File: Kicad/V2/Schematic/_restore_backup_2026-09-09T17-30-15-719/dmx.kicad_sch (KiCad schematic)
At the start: 12 parts, among them J6 XLR5_Ground, U6 B0505S-1W1, U7 6N137, U8 MAX485E

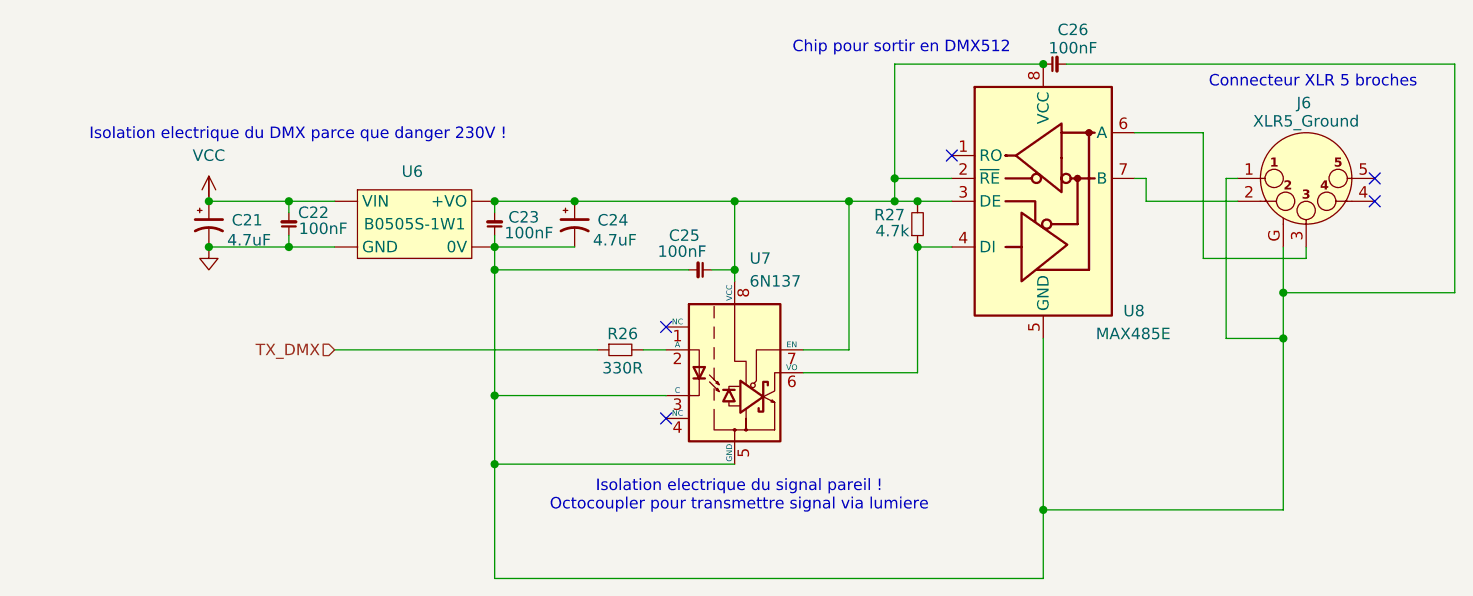
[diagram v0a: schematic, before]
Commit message: finition schematic de reference
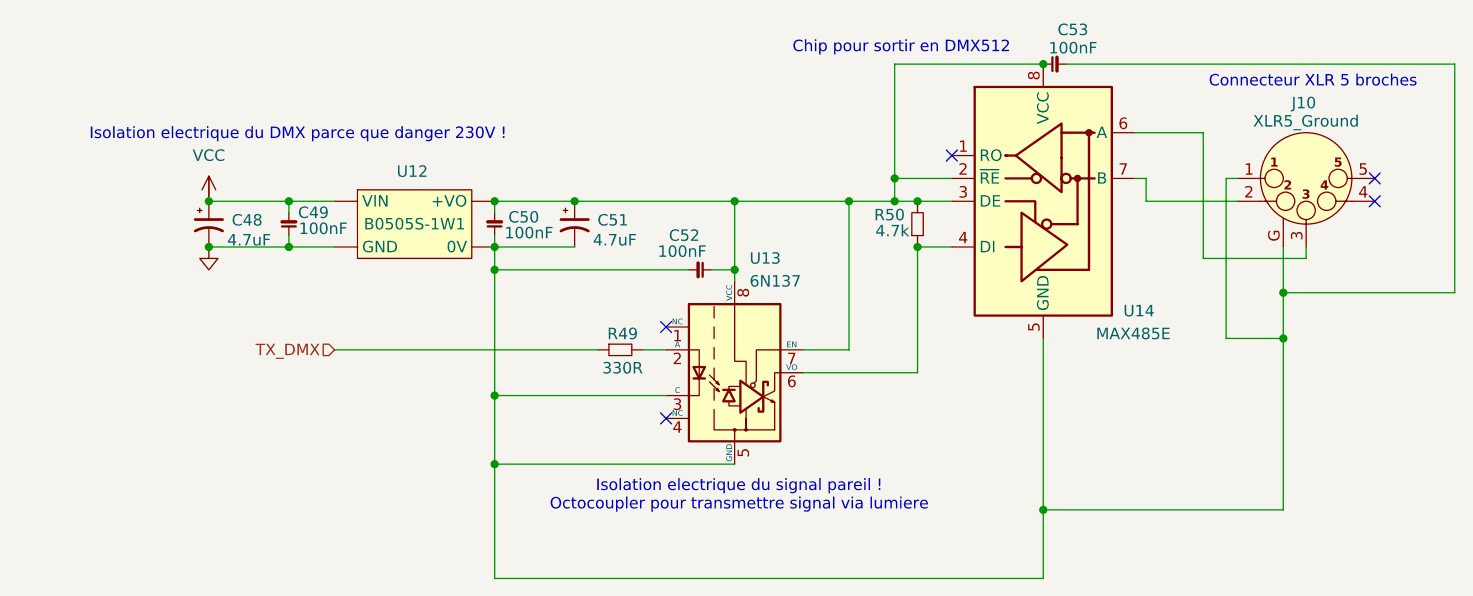
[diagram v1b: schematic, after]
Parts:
- renumbered C21 to C48, C22 to C49, C23 to C50, C24 to C51, C25 to C52, C26 to C53, J6 to J10, R26 to R49, R27 to R50, U6 to U12, U7 to U13, U8 to U14
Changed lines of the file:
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@@
 		(in_pos_files yes)
 		(dnp no)
-		(property "Reference" "J6"
+		(property "Reference" "J10"
 			(at 169.926 71.628 0)
 			(show_name no)
@@
 			(project "G-Love"
 				(path "/808bc5ea-49ac-4454-ba77-8b20d01ce159/bda75adb-ac63-42a7-b1e7-5ba80bc60aa7/a1b0dccf-5d55-40c3-a416-6945c903a7af"
-					(reference "J6")
+					(reference "J10")
 					(unit 1)
 				)
@@
 		(in_pos_files yes)
 		(dnp no)
-		(property "Reference" "C23"
+		(property "Reference" "C50"
 			(at 81.534 84.328 0)
 			(show_name no)
@@
 			(project "G-Love"
 				(path "/808bc5ea-49ac-4454-ba77-8b20d01ce159/bda75adb-ac63-42a7-b1e7-5ba80bc60aa7/a1b0dccf-5d55-40c3-a416-6945c903a7af"
-					(reference "C23")
+					(reference "C50")
 					(unit 1)
 				)
@@
 		(in_pos_files yes)
 		(dnp no)
-		(property "Reference" "R26"
+		(property "Reference" "R49"
 			(at 94.234 97.282 0)
 			(show_name no)
@@
 			(project "G-Love"
 				(path "/808bc5ea-49ac-4454-ba77-8b20d01ce159/bda75adb-ac63-42a7-b1e7-5ba80bc60aa7/a1b0dccf-5d55-40c3-a416-6945c903a7af"
-					(reference "R26")
+					(reference "R49")
 					(unit 1)
 				)
@@
 		(in_pos_files yes)
 		(dnp no)
-		(property "Reference" "C26"
+		(property "Reference" "C53"
 			(at 144.272 63.5 90)
 			(show_name no)
@@
 			(project "G-Love"
 				(path "/808bc5ea-49ac-4454-ba77-8b20d01ce159/bda75adb-ac63-42a7-b1e7-5ba80bc60aa7/a1b0dccf-5d55-40c3-a416-6945c903a7af"
-					(reference "C26")
+					(reference "C53")
 					(unit 1)
 				)
@@
 		(in_pos_files yes)
 		(dnp no)
-		(property "Reference" "C22"
+		(property "Reference" "C49"
 			(at 58.166 83.82 0)
 			(show_name no)
@@
 			(project "G-Love"
 				(path "/808bc5ea-49ac-4454-ba77-8b20d01ce159/bda75adb-ac63-42a7-b1e7-5ba80bc60aa7/a1b0dccf-5d55-40c3-a416-6945c903a7af"
-					(reference "C22")
+					(reference "C49")
 					(unit 1)
 				)
@@
 		(dnp no)
 		(fields_autoplaced yes)
-		(property "Reference" "GND030"
+		(property "Reference" "GND056"
 			(at 48.26 91.186 0)
 			(hide yes)
@@
 			(project "G-Love"
 				(path "/808bc5ea-49ac-4454-ba77-8b20d01ce159/bda75adb-ac63-42a7-b1e7-5ba80bc60aa7/a1b0dccf-5d55-40c3-a416-6945c903a7af"
-					(reference "GND030")
+					(reference "GND056")
 					(unit 1)
 				)
@@
 		(in_pos_files yes)
 		(dnp no)
-		(property "Reference" "C21"
+		(property "Reference" "C48"
 			(at 50.8 84.6581 0)
 			(show_name no)
@@
 			(project "G-Love"
 				(path "/808bc5ea-49ac-4454-ba77-8b20d01ce159/bda75adb-ac63-42a7-b1e7-5ba80bc60aa7/a1b0dccf-5d55-40c3-a416-6945c903a7af"
-					(reference "C21")
+					(reference "C48")
 					(unit 1)
 				)
@@
 		(in_pos_files yes)
 		(dnp no)
-		(property "Reference" "C25"
+		(property "Reference" "C52"
 			(at 101.092 86.36 90)
 			(show_name no)
@@
 			(project "G-Love"
 				(path "/808bc5ea-49ac-4454-ba77-8b20d01ce159/bda75adb-ac63-42a7-b1e7-5ba80bc60aa7/a1b0dccf-5d55-40c3-a416-6945c903a7af"
-					(reference "C25")
+					(reference "C52")
 					(unit 1)
 				)
@@
 		(dnp no)
 		(fields_autoplaced yes)
-		(property "Reference" "U7"
+		(property "Reference" "U13"
 			(at 108.3311 88.9 0)
 			(show_name no)
@@
 			(project "G-Love"
 				(path "/808bc5ea-49ac-4454-ba77-8b20d01ce159/bda75adb-ac63-42a7-b1e7-5ba80bc60aa7/a1b0dccf-5d55-40c3-a416-6945c903a7af"
-					(reference "U7")
+					(reference "U13")
 					(unit 1)
 				)
@@
 		(in_pos_files yes)
 		(dnp no)
-		(property "Reference" "U6"
+		(property "Reference" "U12"
 			(at 70.866 79.248 0)
 			(show_name no)
@@
 			(project "G-Love"
 				(path "/808bc5ea-49ac-4454-ba77-8b20d01ce159/bda75adb-ac63-42a7-b1e7-5ba80bc60aa7/a1b0dccf-5d55-40c3-a416-6945c903a7af"
-					(reference "U6")
+					(reference "U12")
 					(unit 1)
 				)
@@
 		(in_pos_files yes)
 		(dnp no)
-		(property "Reference" "C24"
+		(property "Reference" "C51"
 			(at 91.44 84.6581 0)
 			(show_name no)
@@
 			(project "G-Love"
 				(path "/808bc5ea-49ac-4454-ba77-8b20d01ce159/bda75adb-ac63-42a7-b1e7-5ba80bc60aa7/a1b0dccf-5d55-40c3-a416-6945c903a7af"
-					(reference "C24")
+					(reference "C51")
 					(unit 1)
 				)
@@
 		(dnp no)
 		(fields_autoplaced yes)
-		(property "Reference" "#PWR021"
+		(property "Reference" "#PWR031"
 			(at 52.07 83.058 0)
 			(hide yes)
@@
 			(project "G-Love"
 				(path "/808bc5ea-49ac-4454-ba77-8b20d01ce159/bda75adb-ac63-42a7-b1e7-5ba80bc60aa7/a1b0dccf-5d55-40c3-a416-6945c903a7af"
-					(reference "#PWR021")
+					(reference "#PWR031")
 					(unit 1)
 				)
@@
 		(in_pos_files yes)
 		(dnp no)
-		(property "Reference" "R27"
+		(property "Reference" "R50"
 			(at 122.174 84.074 90)
 			(show_name no)
@@
 			(project "G-Love"
 				(path "/808bc5ea-49ac-4454-ba77-8b20d01ce159/bda75adb-ac63-42a7-b1e7-5ba80bc60aa7/a1b0dccf-5d55-40c3-a416-6945c903a7af"
-					(reference "R27")
+					(reference "R50")
 					(unit 1)
 				)
@@
 		(in_pos_files yes)
 		(dnp no)
-		(property "Reference" "U8"
+		(property "Reference" "U14"
 			(at 149.86 94.742 0)
 			(show_name no)
@@
 			(project "G-Love"
 				(path "/808bc5ea-49ac-4454-ba77-8b20d01ce159/bda75adb-ac63-42a7-b1e7-5ba80bc60aa7/a1b0dccf-5d55-40c3-a416-6945c903a7af"
-					(reference "U8")
+					(reference "U14")
 					(unit 1)
 				)
